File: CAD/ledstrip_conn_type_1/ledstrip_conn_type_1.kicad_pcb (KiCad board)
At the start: 2 copper layers, 22.3 x 19.3 mm, 4 parts, among them J1 led_strip_output, J2 led_strip_input, J3 led_strip_input

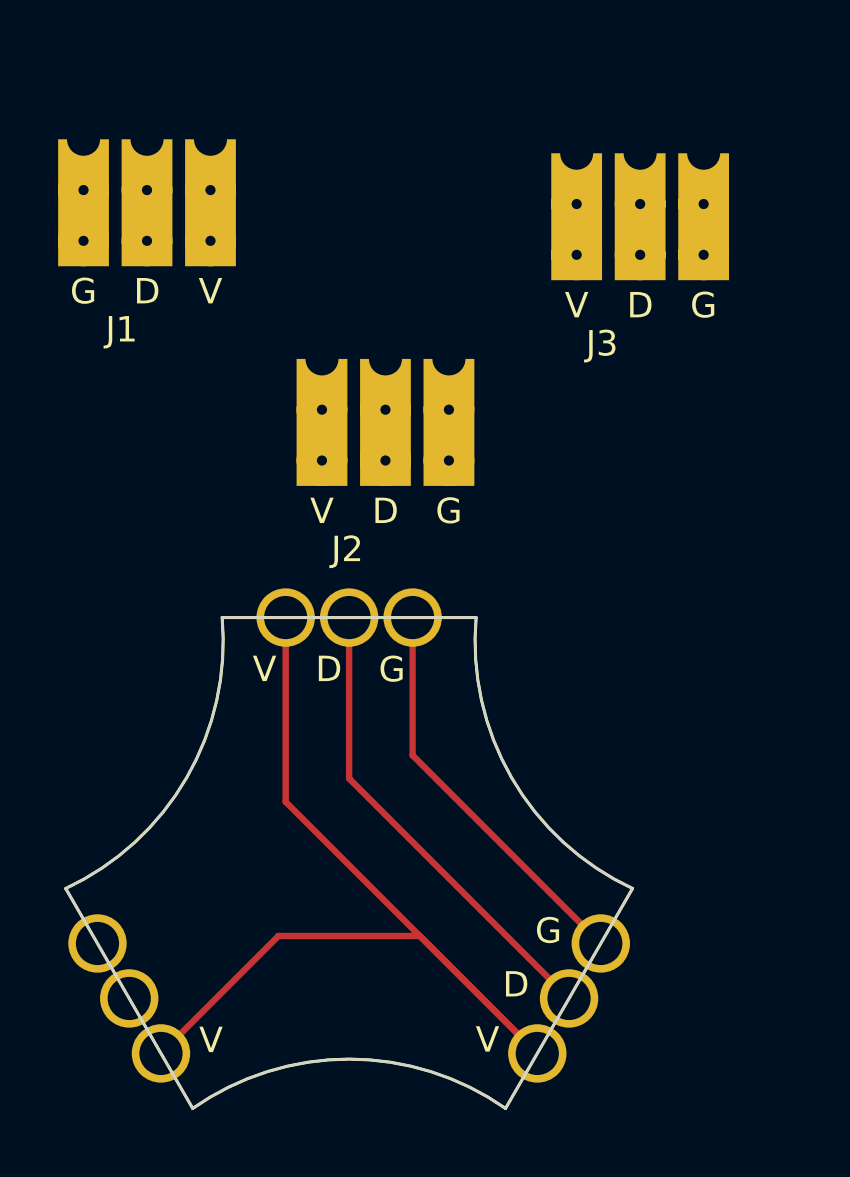
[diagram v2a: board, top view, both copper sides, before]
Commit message: Feat: New design, single connector
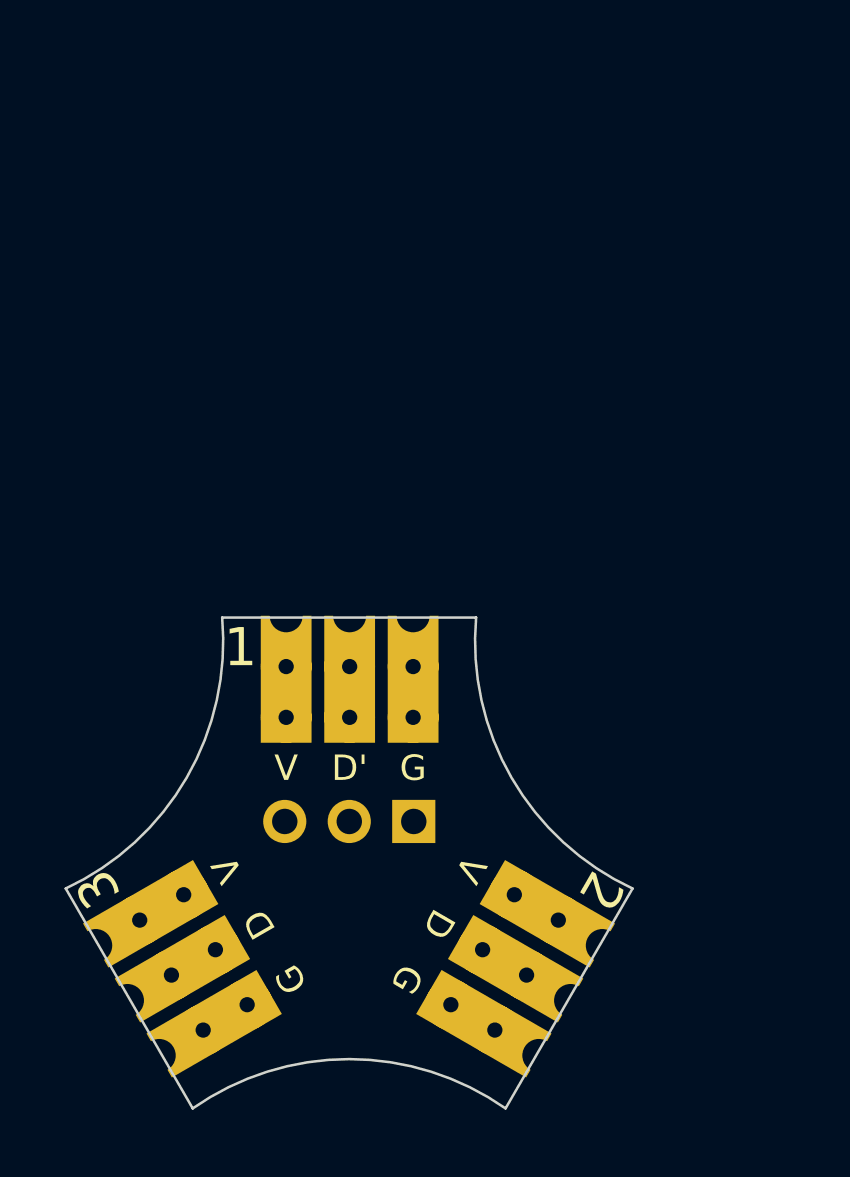
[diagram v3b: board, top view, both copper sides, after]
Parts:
- removed REF**: led_cube, Connector:led_cube
- added J4: Conn_01x03, Connector_PinHeader_2.54mm:PinHeader_1x03_P2.54mm_Vertical, B.Cu at (147.3, 107.2)
- moved J1 33.9 mm to (136.1, 114.3), turned to 120 degrees
- moved J3 33.5 mm to (153.5, 114.3), turned to -120 degrees
- moved J2 10.2 mm to (144.8, 99.2)
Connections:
- net Net-(J1-Pad1) renamed /V
- net Net-(J1-Pad2) renamed /D
- J1 pad 3: Net-(J1-Pad3) -> /G
- J2 pad 2: unconnected-(J2-Pad2) -> /D'
- J2 pad 3: unconnected-(J2-Pad3) -> /G
- J3 pad 3: Net-(J1-Pad3) -> /G
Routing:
- net (no net): track 74.4 -> 0.00 mm
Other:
- board text added: "1"
- board text added: "2"
- board text added: "3"
- board text added: "4"
- board text added: "5"
- board text added: "6"
- board text removed: "D"
- board text removed: "G"
- board text removed: "V"

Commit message: feat: added wires to pcb
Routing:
- net /G: track 0.00 -> 35.4 mm
- net /V: track 0.00 -> 32.1 mm
- net /D: track 0.00 -> 18.6 mm
- net /D': track 0.00 -> 11.7 mm
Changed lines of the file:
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@@
     (effects (font (size 1.5 1.5) (thickness 0.3)))
   )
+  (segment (start 151.285898 110.134936) (end 142.384936 110.134936) (width 0.25) (layer "F.Cu") (net 1))
+  (segment (start 142.384936 110.134936) (end 142.245 109.995) (width 0.25) (layer "F.Cu") (net 1))
+  (segment (start 142.245 99.4) (end 142.3 99.345) (width 0.25) (layer "F.Cu") (net 1))
+  (segment (start 142.245 107.25) (end 142.245 103.205) (width 0.25) (layer "F.Cu") (net 1))
+  (segment (start 153.177431 112.026469) (end 154.562135 112.026469) (width 0.25) (layer "F.Cu") (net 1))
+  (segment (start 142.3 103.15) (end 142.3 99.345) (width 0.25) (layer "F.Cu") (net 1))
+  (segment (start 151.285898 110.134936) (end 153.177431 112.026469) (width 0.25) (layer "F.Cu") (net 1))
+  (segment (start 142.245 103.205) (end 142.3 103.15) (width 0.25) (layer "F.Cu") (net 1))
+  (segment (start 142.384936 110.134936) (end 138.264102 110.134936) (width 0.25) (layer "F.Cu") (net 1))
+  (segment (start 136.3769 112.022138) (end 134.995366 112.022138) (width 0.25) (layer "F.Cu") (net 1))
+  (segment (start 142.245 109.995) (end 142.245 107.25) (width 0.25) (layer "F.Cu") (net 1))
+  (segment (start 138.264102 110.134936) (end 136.3769 112.022138) (width 0.25) (layer "F.Cu") (net 1))
+  (segment (start 150.035898 112.3) (end 151.927415 114.191517) (width 0.25) (layer "F.Cu") (net 2))
+  (segment (start 139.514102 112.3) (end 137.626915 114.187187) (width 0.25) (layer "F.Cu") (net 2))
+  (segment (start 150.035898 112.3) (end 139.514102 112.3) (width 0.25) (layer "F.Cu") (net 2))
+  (segment (start 151.927415 114.191517) (end 153.312108 114.191517) (width 0.25) (layer "F.Cu") (net 2))
+  (segment (start 137.626915 114.187187) (end 136.245393 114.187187) (width 0.25) (layer "F.Cu") (net 2))
+  (segment (start 147.325 99.37) (end 147.3 99.345) (width 0.25) (layer "F.Cu") (net 3))
+  (segment (start 146.565064 114.465064) (end 147.325 113.705128) (width 0.25) (layer "B.Cu") (net 3))
+  (segment (start 148.785898 114.465064) (end 150.677399 116.356565) (width 0.25) (layer "B.Cu") (net 3))
+  (segment (start 150.677399 116.356565) (end 152.062079 116.356565) (width 0.25) (layer "B.Cu") (net 3))
+  (segment (start 147.325 113.705128) (end 147.325 107.25) (width 0.25) (layer "B.Cu") (net 3))
+  (segment (start 138.723855 116.505311) (end 137.583802 116.505311) (width 0.25) (layer "B.Cu") (net 3))
+  (segment (start 147.3 103.15) (end 147.3 99.345) (width 0.25) (layer "B.Cu") (net 3))
+  (segment (start 147.325 107.25) (end 147.325 99.37) (width 0.25) (layer "B.Cu") (net 3))
+  (segment (start 148.785898 114.465064) (end 146.565064 114.465064) (width 0.25) (layer "B.Cu") (net 3))
+  (segment (start 146.565064 114.465064) (end 140.764102 114.465064) (width 0.25) (layer "B.Cu") (net 3))
+  (segment (start 138.723855 116.505311) (end 140.764102 114.465064) (width 0.25) (layer "B.Cu") (net 3))
+  (segment (start 144.785 99.36) (end 144.8 99.345) (width 0.25) (layer "F.Cu") (net 4))
+  (segment (start 144.785 107.25) (end 144.785 99.36) (width 0.25) (layer "B.Cu") (net 4))
+  (segment (start 144.8 103.15) (end 144.8 99.345) (width 0.25) (layer "B.Cu") (net 4))
 )

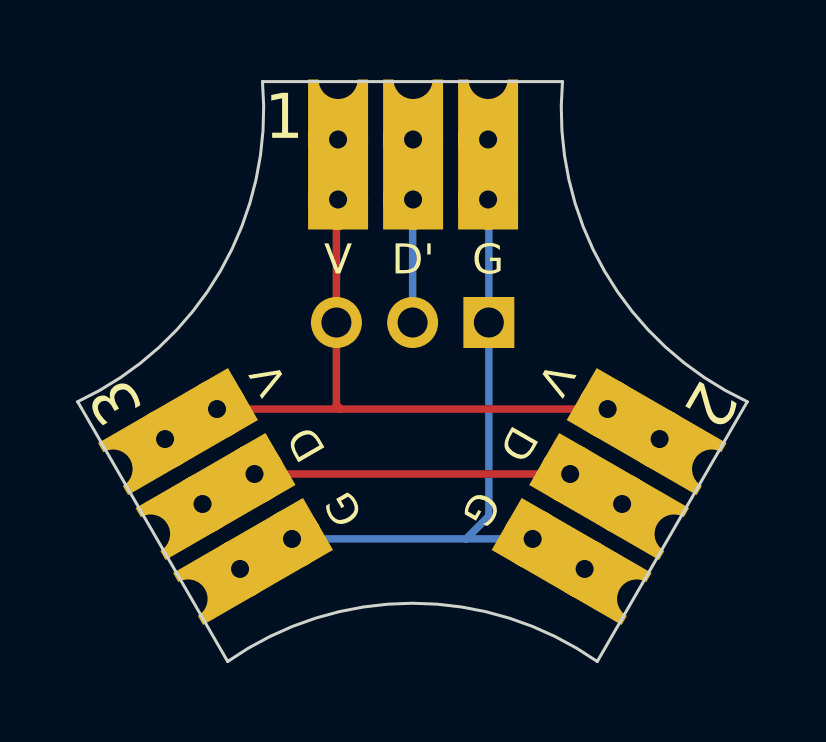
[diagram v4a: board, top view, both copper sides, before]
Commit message: Feat:Changed tracewidth, added pictures, prodfiles
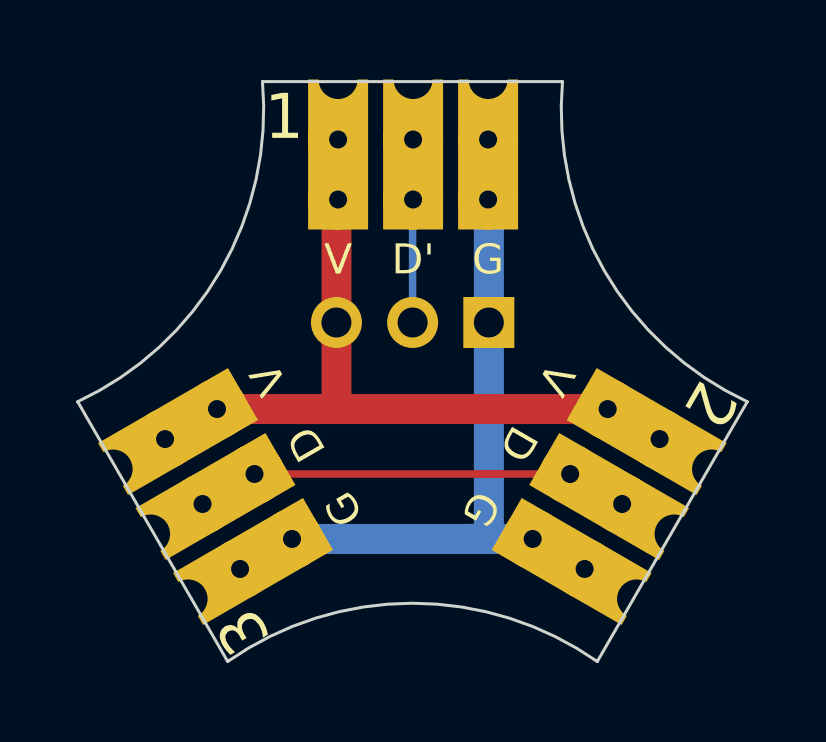
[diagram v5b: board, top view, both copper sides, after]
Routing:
- net /V: track 32.1 -> 24.0 mm
- net /G: track 35.4 -> 27.7 mm
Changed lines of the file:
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@@
     (effects (font (size 1.5 1.5) (thickness 0.3)) (justify mirror))
   )
-  (gr_text "6\n" (at 139.2 117.4 120) (layer "B.SilkS")
+  (gr_text "6\n" (at 134.8 110 120) (layer "B.SilkS")
     (effects (font (size 1.5 1.5) (thickness 0.3)))
   )
@@
     (effects (font (size 1.5 1.5) (thickness 0.3)))
   )
-  (gr_text "3" (at 134.9 109.9 120) (layer "F.SilkS")
+  (gr_text "3" (at 139.15 117.55 120) (layer "F.SilkS")
     (effects (font (size 1.5 1.5) (thickness 0.3)))
   )
@@
     (effects (font (size 1.5 1.5) (thickness 0.3)))
   )
-  (segment (start 151.285898 110.134936) (end 142.384936 110.134936) (width 0.25) (layer "F.Cu") (net 1))
-  (segment (start 142.384936 110.134936) (end 142.245 109.995) (width 0.25) (layer "F.Cu") (net 1))
-  (segment (start 142.245 99.4) (end 142.3 99.345) (width 0.25) (layer "F.Cu") (net 1))
-  (segment (start 142.245 107.25) (end 142.245 103.205) (width 0.25) (layer "F.Cu") (net 1))
-  (segment (start 153.177431 112.026469) (end 154.562135 112.026469) (width 0.25) (layer "F.Cu") (net 1))
-  (segment (start 142.3 103.15) (end 142.3 99.345) (width 0.25) (layer "F.Cu") (net 1))
-  (segment (start 151.285898 110.134936) (end 153.177431 112.026469) (width 0.25) (layer "F.Cu") (net 1))
-  (segment (start 142.245 103.205) (end 142.3 103.15) (width 0.25) (layer "F.Cu") (net 1))
-  (segment (start 142.384936 110.134936) (end 138.264102 110.134936) (width 0.25) (layer "F.Cu") (net 1))
-  (segment (start 136.3769 112.022138) (end 134.995366 112.022138) (width 0.25) (layer "F.Cu") (net 1))
-  (segment (start 142.245 109.995) (end 142.245 107.25) (width 0.25) (layer "F.Cu") (net 1))
-  (segment (start 138.264102 110.134936) (end 136.3769 112.022138) (width 0.25) (layer "F.Cu") (net 1))
+  (segment (start 151.285898 110.134936) (end 142.384936 110.134936) (width 1) (layer "F.Cu") (net 1))
+  (segment (start 142.384936 110.134936) (end 142.245 109.995) (width 1) (layer "F.Cu") (net 1))
+  (segment (start 142.245 99.4) (end 142.3 99.345) (width 1) (layer "F.Cu") (net 1))
+  (segment (start 142.245 107.25) (end 142.245 103.205) (width 1) (layer "F.Cu") (net 1))
+  (segment (start 142.3 103.15) (end 142.3 99.345) (width 1) (layer "F.Cu") (net 1))
+  (segment (start 142.245 103.205) (end 142.3 103.15) (width 1) (layer "F.Cu") (net 1))
+  (segment (start 142.384936 110.134936) (end 138.264102 110.134936) (width 1) (layer "F.Cu") (net 1))
+  (segment (start 142.245 109.995) (end 142.245 107.25) (width 1) (layer "F.Cu") (net 1))
   (segment (start 150.035898 112.3) (end 151.927415 114.191517) (width 0.25) (layer "F.Cu") (net 2))
   (segment (start 139.514102 112.3) (end 137.626915 114.187187) (width 0.25) (layer "F.Cu") (net 2))
@@
   (segment (start 137.626915 114.187187) (end 136.245393 114.187187) (width 0.25) (layer "F.Cu") (net 2))
   (segment (start 147.325 99.37) (end 147.3 99.345) (width 0.25) (layer "F.Cu") (net 3))
-  (segment (start 146.565064 114.465064) (end 147.325 113.705128) (width 0.25) (layer "B.Cu") (net 3))
-  (segment (start 148.785898 114.465064) (end 150.677399 116.356565) (width 0.25) (layer "B.Cu") (net 3))
-  (segment (start 150.677399 116.356565) (end 152.062079 116.356565) (width 0.25) (layer "B.Cu") (net 3))
-  (segment (start 147.325 113.705128) (end 147.325 107.25) (width 0.25) (layer "B.Cu") (net 3))
-  (segment (start 138.723855 116.505311) (end 137.583802 116.505311) (width 0.25) (layer "B.Cu") (net 3))
+  (segment (start 146.565064 114.465064) (end 147.300733 114.465064) (width 1) (layer "B.Cu") (net 3))
+  (segment (start 147.300733 114.465064) (end 147.325 114.440797) (width 1) (layer "B.Cu") (net 3))
   (segment (start 147.3 103.15) (end 147.3 99.345) (width 0.25) (layer "B.Cu") (net 3))
-  (segment (start 147.325 107.25) (end 147.325 99.37) (width 0.25) (layer "B.Cu") (net 3))
-  (segment (start 148.785898 114.465064) (end 146.565064 114.465064) (width 0.25) (layer "B.Cu") (net 3))
-  (segment (start 146.565064 114.465064) (end 140.764102 114.465064) (width 0.25) (layer "B.Cu") (net 3))
-  (segment (start 138.723855 116.505311) (end 140.764102 114.465064) (width 0.25) (layer "B.Cu") (net 3))
+  (segment (start 147.325 107.25) (end 147.325 99.37) (width 1) (layer "B.Cu") (net 3))
+  (segment (start 147.325 114.440797) (end 147.325 107.25) (width 1) (layer "B.Cu") (net 3))
+  (segment (start 148.785898 114.465064) (end 146.565064 114.465064) (width 1) (layer "B.Cu") (net 3))
+  (segment (start 146.565064 114.465064) (end 140.764102 114.465064) (width 1) (layer "B.Cu") (net 3))
   (segment (start 144.785 99.36) (end 144.8 99.345) (width 0.25) (layer "F.Cu") (net 4))
   (segment (start 144.785 107.25) (end 144.785 99.36) (width 0.25) (layer "B.Cu") (net 4))

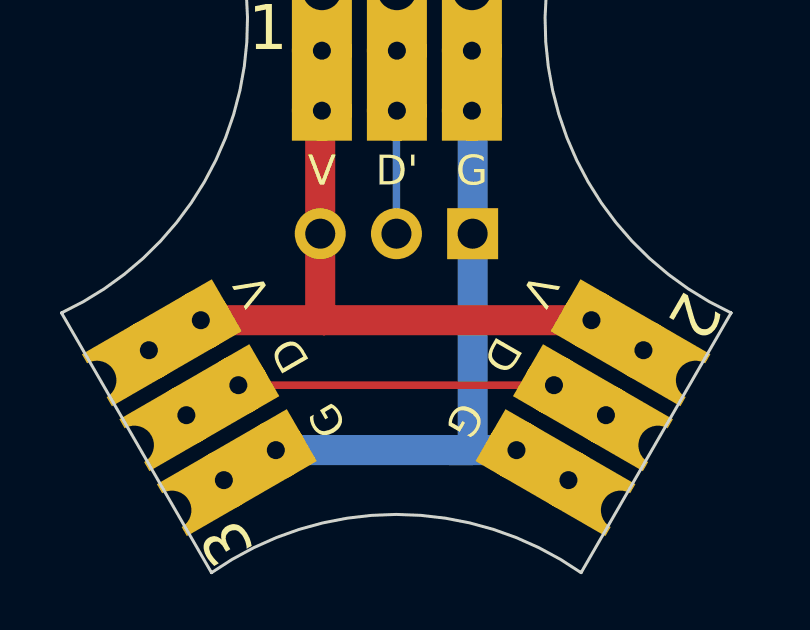
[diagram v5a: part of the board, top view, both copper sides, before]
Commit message: feat: added personal customization to pcb
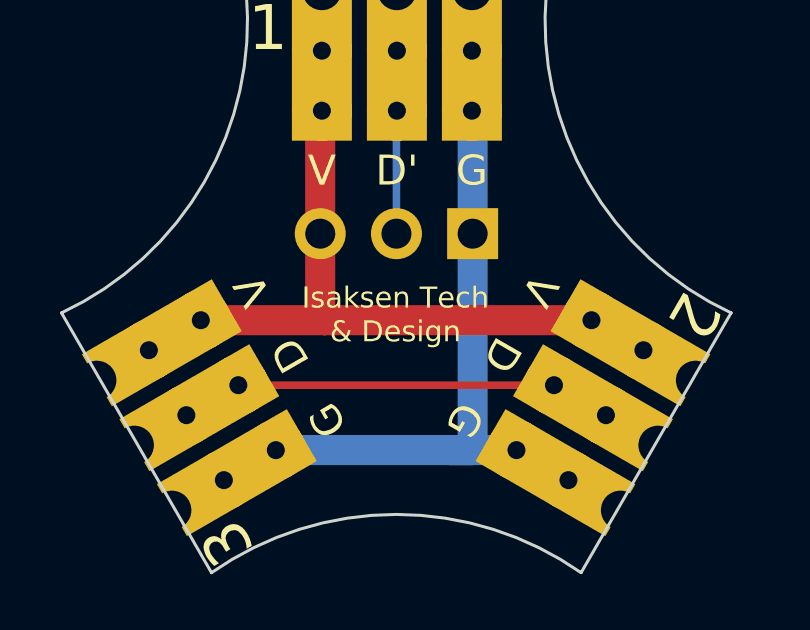
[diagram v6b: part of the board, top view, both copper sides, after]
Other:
- board text added: "Isaksen Tech & Design"
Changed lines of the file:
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@@
     (effects (font (size 1.5 1.5) (thickness 0.3)) (justify mirror))
+  )
+  (gr_text "Isaksen Tech\n& Design" (at 144.75 109.95) (layer "B.SilkS")
+    (effects (font (size 0.7 0.7) (thickness 0.15)) (justify mirror))
   )
   (gr_text "6\n" (at 134.8 110 120) (layer "B.SilkS")
@@
     (effects (font (size 1.5 1.5) (thickness 0.3)))
   )
+  (gr_text "Isaksen Tech\n& Design" (at 144.75 109.95) (layer "F.SilkS")
+    (effects (font (size 0.7 0.7) (thickness 0.15)))
+  )
   (gr_text "3" (at 139.15 117.55 120) (layer "F.SilkS")
